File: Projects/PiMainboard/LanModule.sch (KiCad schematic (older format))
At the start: 0 parts

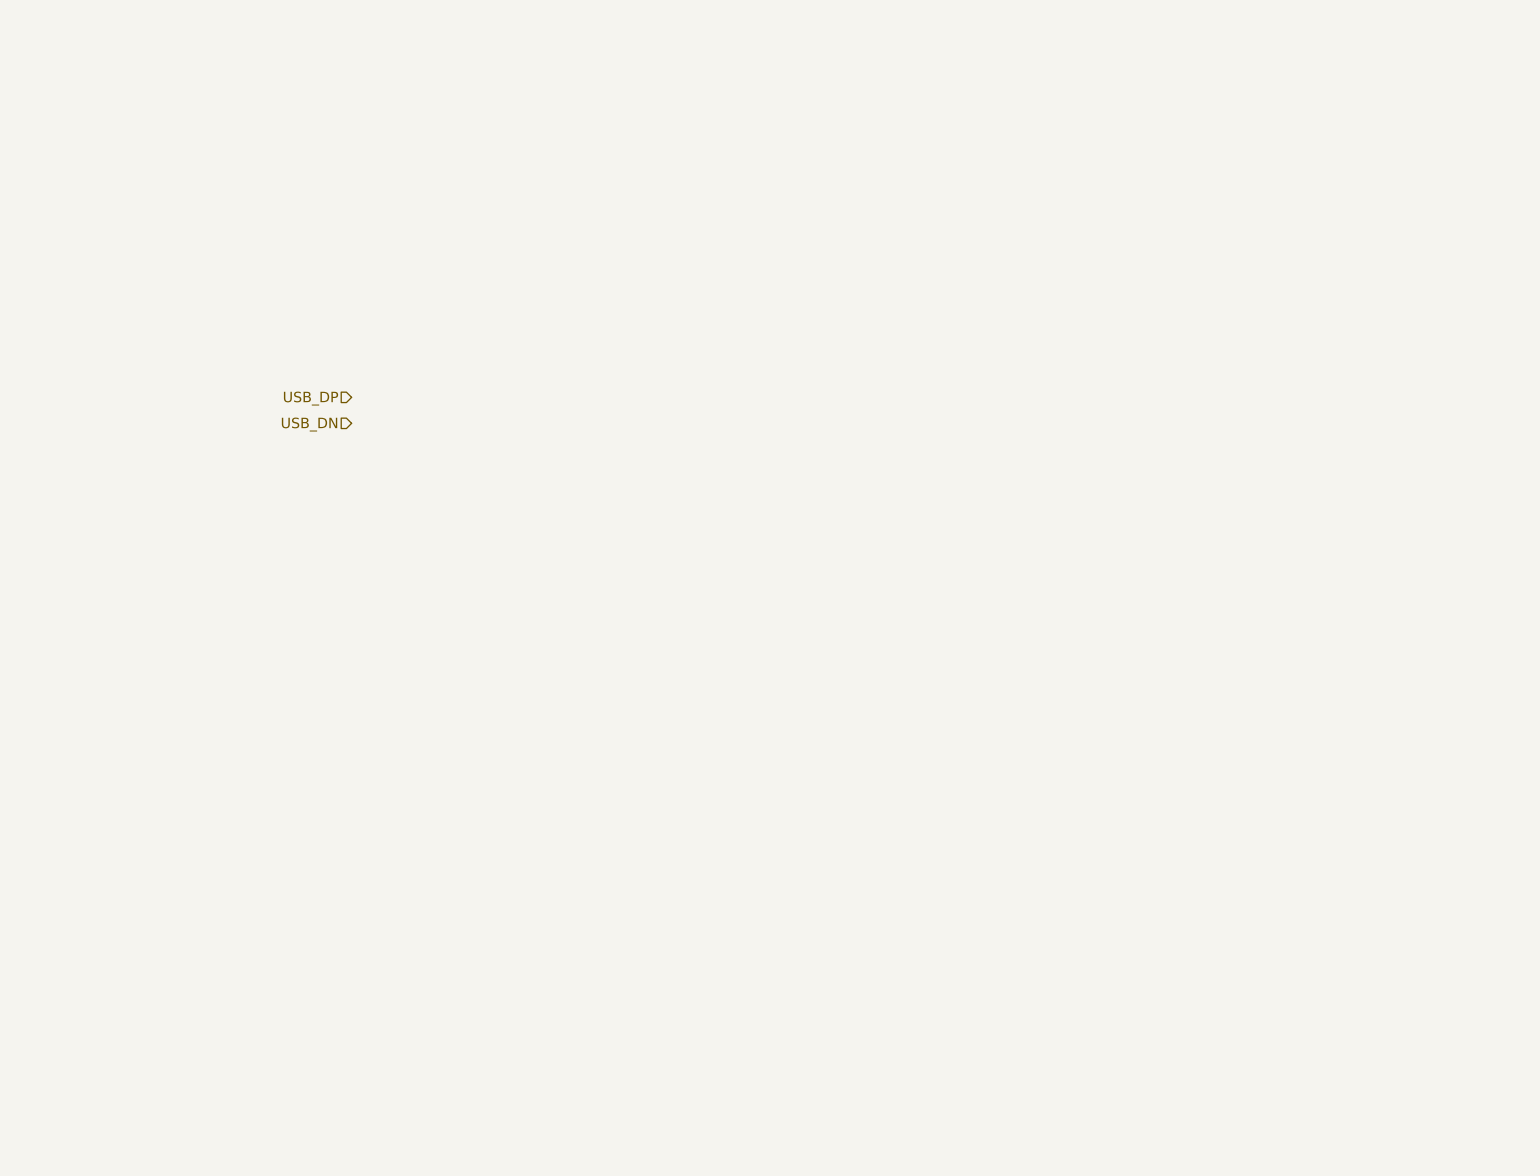
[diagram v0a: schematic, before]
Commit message: Added LAN to Pi board
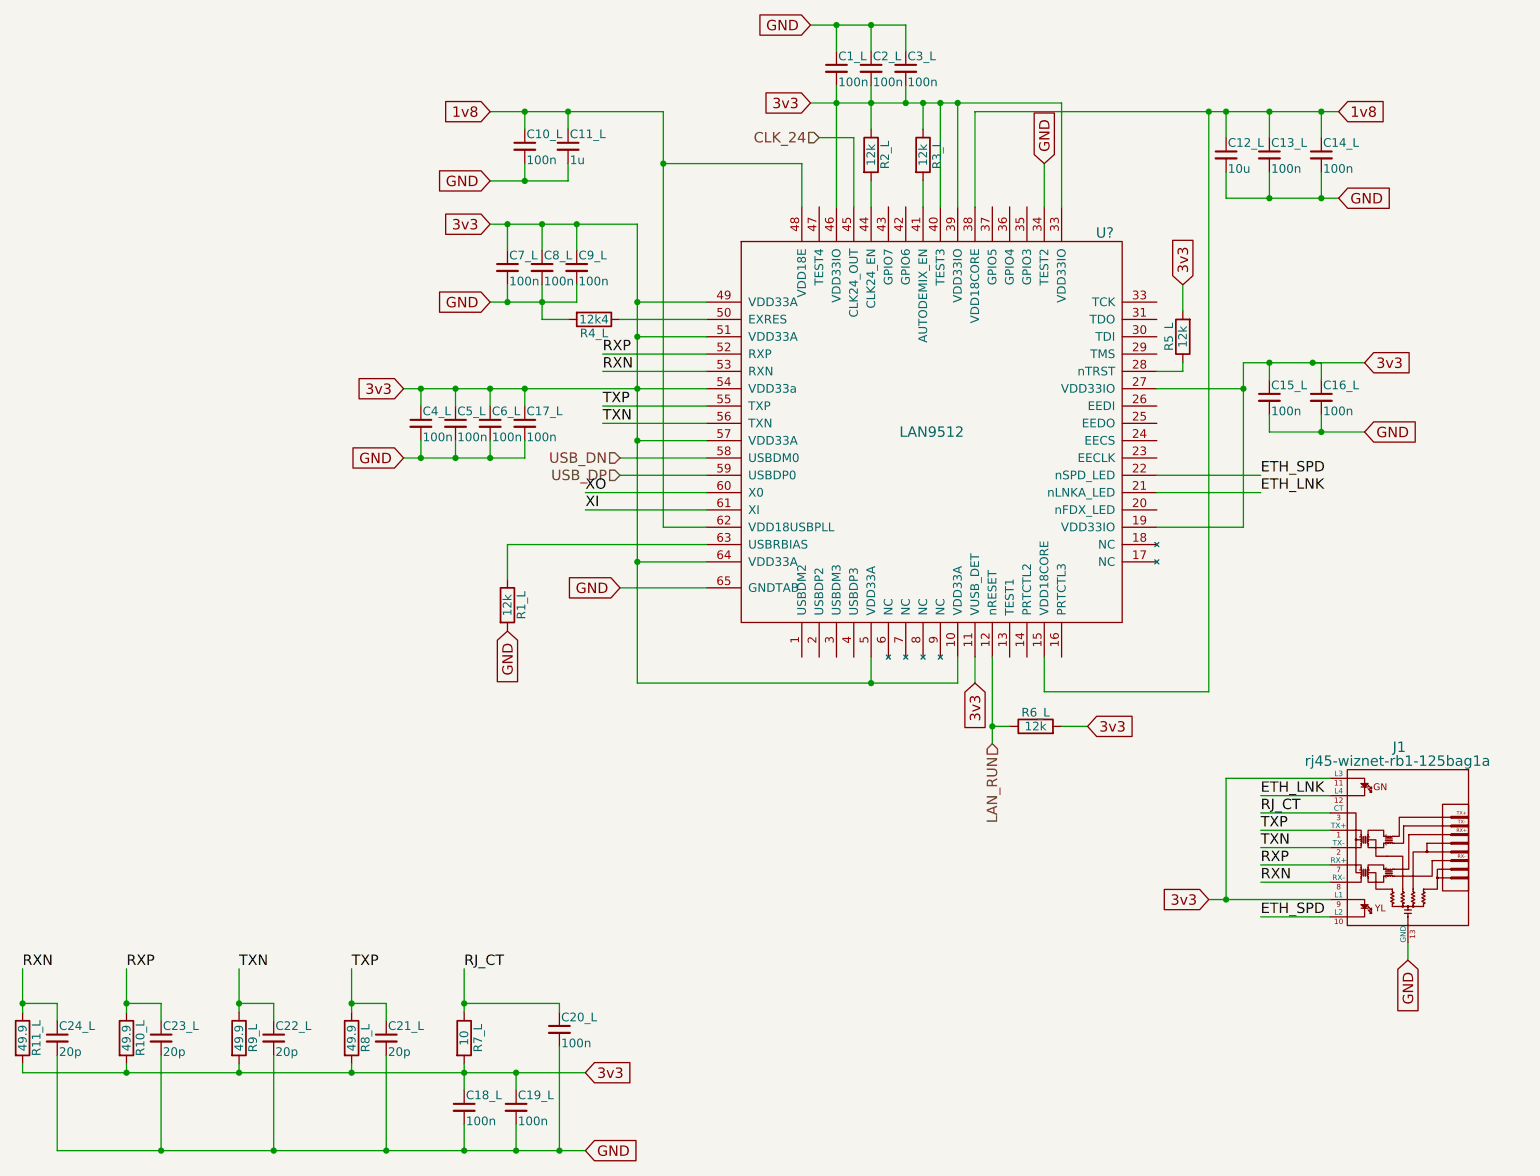
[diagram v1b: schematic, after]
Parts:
- added C10_L, C13_L, C14_L, C15_L, C16_L, C17_L, C18_L, C19_L, C1_L, C20_L, C2_L, C3_L, C4_L, C5_L, C6_L, C7_L, C8_L, C9_L: 100n, symbol C_Small
- added C11_L: 1u, symbol C_Small
- added C12_L: 10u, symbol C_Small
- added C21_L, C22_L, C23_L, C24_L: 20p, symbol C_Small
- added J1: rj45-wiznet-rb1-125bag1a, symbol rj45-wiznet-rb1-125bag1a
- added R10_L, R11_L, R8_L, R9_L: 49.9, symbol R
- added R1_L, R2_L, R3_L, R5_L, R6_L: 12k, symbol R
- added R4_L: 12k4, symbol R
- added R7_L: 10, symbol R
- added U?: LAN9512, symbol LAN9512
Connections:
- net USB_DN: now also U?.58 (USBDM0)
- net USB_DP: now also U?.59 (USBDP0)
- new net: R5_L.1, U?.28 (nTRST)
- new net: R3_L.2, U?.41 (AUTODEMIX_EN)
- new net: R2_L.2, U?.44 (CLK24_EN)
- new net: R4_L.1, U?.50 (EXRES)
- new net: R1_L.1, U?.63 (USBRBIAS)
- new net 1v8: C10_L.1, C11_L.1, C12_L.1, C13_L.1, C14_L.1, U?.15 (VDD18CORE), U?.38 (VDD18CORE), U?.48 (VDD18E), U?.62 (VDD18USBPLL)
- new net 3v3: C15_L.1, C16_L.1, C17_L.1, C18_L.1, C19_L.1, C1_L.2, C2_L.2, C3_L.2, C4_L.1, C5_L.1, C6_L.1, C7_L.1, C8_L.1, C9_L.1, J1.11 (L3), J1.9 (L1), R10_L.2, R11_L.2, R2_L.1, R3_L.1, R5_L.2, R6_L.2, R7_L.2, R8_L.2, R9_L.2, U?.10 (VDD33A), U?.11 (VUSB_DET), U?.19 (VDD33IO), U?.27 (VDD33IO), U?.33 (VDD33IO), U?.39 (VDD33IO), U?.40 (TEST3), U?.46 (VDD33IO), U?.49 (VDD33A), U?.5 (VDD33A), U?.51 (VDD33A), U?.54 (VDD33a), U?.57 (VDD33A), U?.64 (VDD33A)
- new net CLK_24: U?.45 (CLK24_OUT)
- new net ETH_LNK: J1.12 (L4), U?.21 (nLNKA_LED)
- new net ETH_SPD: J1.10 (L2), U?.22 (nSPD_LED)
- new net GND: C10_L.2, C11_L.2, C12_L.2, C13_L.2, C14_L.2, C15_L.2, C16_L.2, C17_L.2, C18_L.2, C19_L.2, C1_L.1, C20_L.2, C21_L.2, C22_L.2, C23_L.2, C24_L.2, C2_L.1, C3_L.1, C4_L.2, C5_L.2, C6_L.2, C7_L.2, C8_L.2, C9_L.2, J1.13 (GND), R1_L.2, R4_L.2, U?.34 (TEST2), U?.65 (GNDTAB)
- new net LAN_RUN: R6_L.1, U?.12 (nRESET)
- new net RJ_CT: C20_L.1, J1.3 (CT), R7_L.1
- new net RXN: C24_L.1, J1.8 (RX-), R11_L.1, U?.53 (RXN)
- new net RXP: C23_L.1, J1.7 (RX+), R10_L.1, U?.52 (RXP)
- new net TXN: C22_L.1, J1.2 (TX-), R9_L.1, U?.56 (TXN)
- new net TXP: C21_L.1, J1.1 (TX+), R8_L.1, U?.55 (TXP)
- new net XI: U?.61 (XI)
- new net XO: U?.60 (X0)

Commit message: Added PI CM IO "shield"
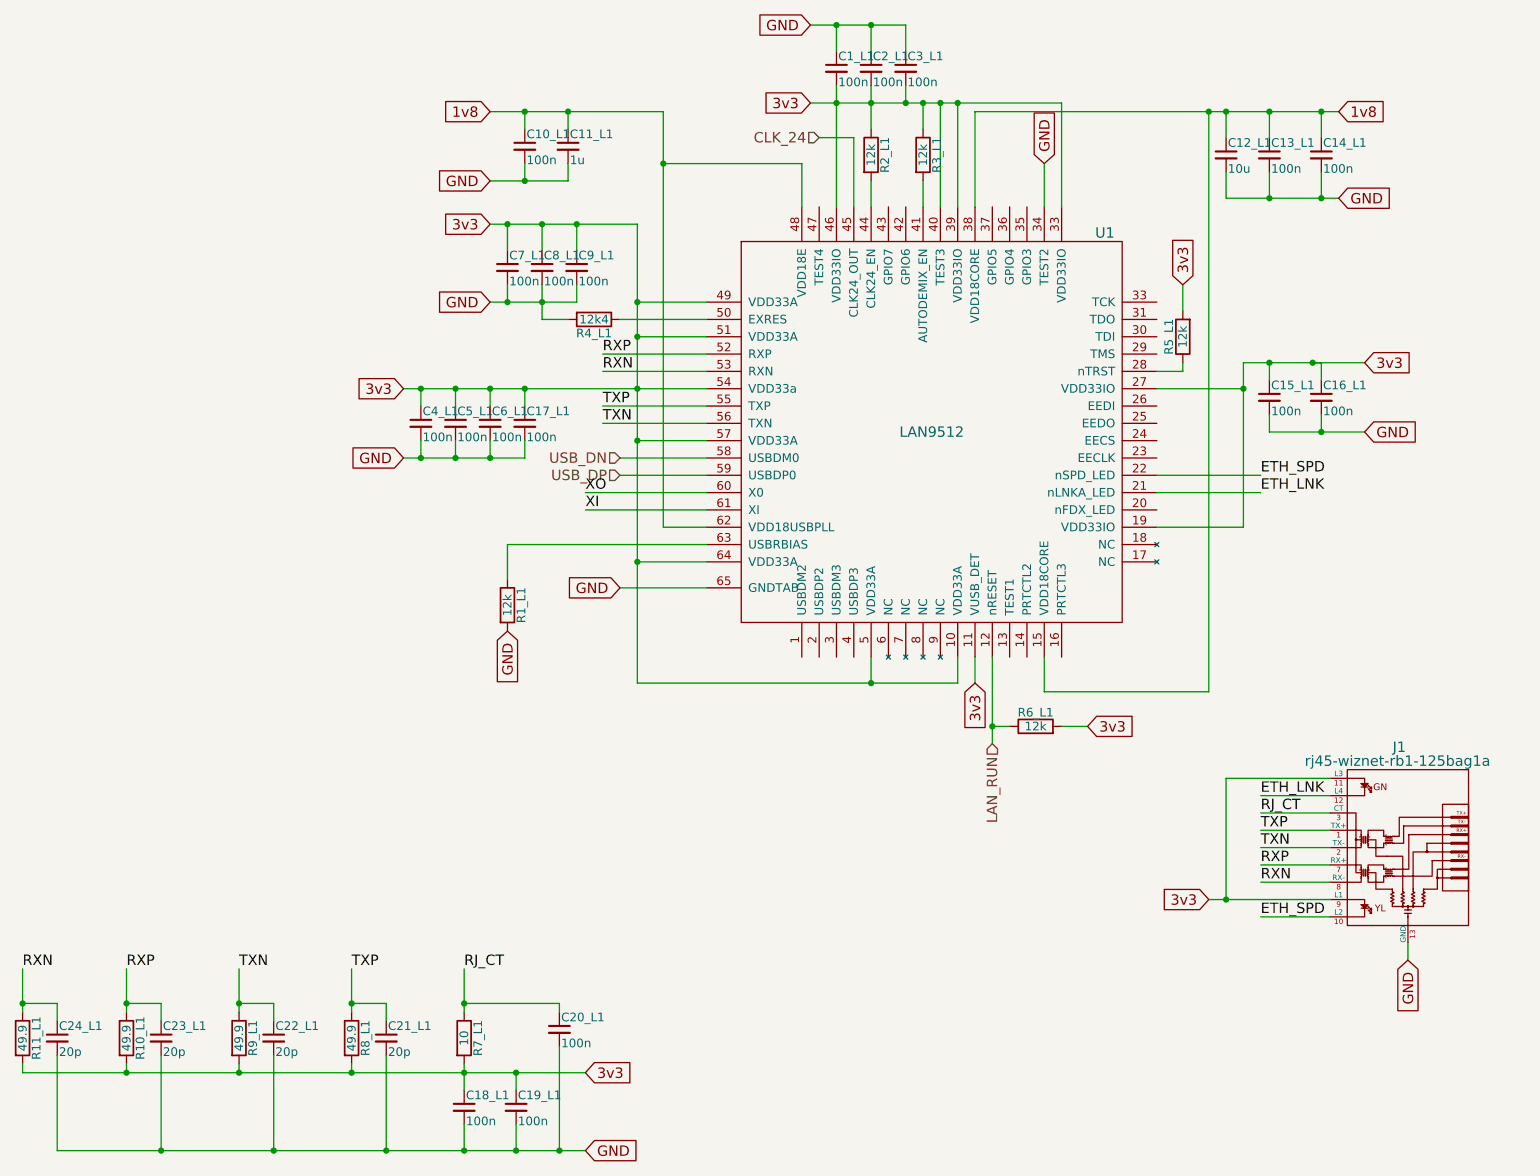
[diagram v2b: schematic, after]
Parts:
- gave numbers to parts that had none: 1
- renumbered C10_L to C10_L1, C11_L to C11_L1, C12_L to C12_L1, C13_L to C13_L1, C14_L to C14_L1, C15_L to C15_L1, C16_L to C16_L1, C17_L to C17_L1, C18_L to C18_L1, C19_L to C19_L1, C1_L to C1_L1, C20_L to C20_L1, C21_L to C21_L1, C22_L to C22_L1, C23_L to C23_L1, C24_L to C24_L1, C2_L to C2_L1, C3_L to C3_L1, C4_L to C4_L1, C5_L to C5_L1, C6_L to C6_L1, C7_L to C7_L1, C8_L to C8_L1, C9_L to C9_L1, R10_L to R10_L1, R11_L to R11_L1, R1_L to R1_L1, R2_L to R2_L1, R3_L to R3_L1, R4_L to R4_L1, R5_L to R5_L1, R6_L to R6_L1, R7_L to R7_L1, R8_L to R8_L1, R9_L to R9_L1
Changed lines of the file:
@@
 $Descr A4 11693 8268
 encoding utf-8
-Sheet 2 7
+Sheet 2 10
 Title ""
 Date ""
@@
 USB_DN
 $Comp
-L LAN9512 U?
+L LAN9512 U1
 U 1 1 567BBE0D
 P 7650 3000
-F 0 "U?" H 8650 4150 60  0000 C CNN
+F 0 "U1" H 8650 4150 60  0000 C CNN
 F 1 "LAN9512" H 7650 3000 60  0000 C CNN
 F 2 "" H 8100 2750 60  0000 C CNN
@@
 LAN_RUN
 $Comp
-L C_Small C1_L
+L C_Small C1_L1
 U 1 1 567BCBC3
 P 7100 900
-F 0 "C1_L" H 7110 970 50  0000 L CNN
+F 0 "C1_L1" H 7110 970 50  0000 L CNN
 F 1 "100n" H 7110 820 50  0000 L CNN
 F 2 "" H 7100 900 60  0000 C CNN
@@
 $EndComp
 $Comp
-L C_Small C2_L
+L C_Small C2_L1
 U 1 1 567BCC4E
 P 7300 900
-F 0 "C2_L" H 7310 970 50  0000 L CNN
+F 0 "C2_L1" H 7310 970 50  0000 L CNN
 F 1 "100n" H 7310 820 50  0000 L CNN
 F 2 "" H 7300 900 60  0000 C CNN
@@
 $EndComp
 $Comp
-L C_Small C3_L
+L C_Small C3_L1
 U 1 1 567BCC7D
 P 7500 900
-F 0 "C3_L" H 7510 970 50  0000 L CNN
+F 0 "C3_L1" H 7510 970 50  0000 L CNN
 F 1 "100n" H 7510 820 50  0000 L CNN
 F 2 "" H 7500 900 60  0000 C CNN
@@
 GND
 $Comp
-L C_Small C4_L
+L C_Small C4_L1
 U 1 1 567BD4D0
 P 4700 2950
-F 0 "C4_L" H 4710 3020 50  0000 L CNN
+F 0 "C4_L1" H 4710 3020 50  0000 L CNN
 F 1 "100n" H 4710 2870 50  0000 L CNN
 F 2 "" H 4700 2950 60  0000 C CNN
@@
 $EndComp
 $Comp
-L C_Small C5_L
+L C_Small C5_L1
 U 1 1 567BD563
 P 4900 2950
-F 0 "C5_L" H 4910 3020 50  0000 L CNN
+F 0 "C5_L1" H 4910 3020 50  0000 L CNN
 F 1 "100n" H 4910 2870 50  0000 L CNN
 F 2 "" H 4900 2950 60  0000 C CNN
@@
 $EndComp
 $Comp
-L C_Small C6_L
+L C_Small C6_L1
 U 1 1 567BD5AE
 P 5100 2950
-F 0 "C6_L" H 5110 3020 50  0000 L CNN
+F 0 "C6_L1" H 5110 3020 50  0000 L CNN
 F 1 "100n" H 5110 2870 50  0000 L CNN
 F 2 "" H 5100 2950 60  0000 C CNN
@@
 GND
 $Comp
-L R R1_L
+L R R1_L1
 U 1 1 567BDB10
 P 5200 4000
-F 0 "R1_L" V 5280 4000 50  0000 C CNN
+F 0 "R1_L1" V 5280 4000 50  0000 C CNN
 F 1 "12k" V 5200 4000 50  0000 C CNN
 F 2 "" V 5130 4000 30  0000 C CNN
@@
 3v3
 $Comp
-L R R3_L
+L R R3_L1
 U 1 1 567BE6EE
 P 7600 1400
-F 0 "R3_L" V 7680 1400 50  0000 C CNN
+F 0 "R3_L1" V 7680 1400 50  0000 C CNN
 F 1 "12k" V 7600 1400 50  0000 C CNN
 F 2 "" V 7530 1400 30  0000 C CNN
@@
 $EndComp
 $Comp
-L R R2_L
+L R R2_L1
 U 1 1 567BE7AA
 P 7300 1400
-F 0 "R2_L" V 7380 1400 50  0000 C CNN
+F 0 "R2_L1" V 7380 1400 50  0000 C CNN
 F 1 "12k" V 7300 1400 50  0000 C CNN
 F 2 "" V 7230 1400 30  0000 C CNN
@@
 $EndComp
 $Comp
-L C_Small C7_L
+L C_Small C7_L1
 U 1 1 567BF03B
 P 5200 2050
-F 0 "C7_L" H 5210 2120 50  0000 L CNN
+F 0 "C7_L1" H 5210 2120 50  0000 L CNN
 F 1 "100n" H 5210 1970 50  0000 L CNN
 F 2 "" H 5200 2050 60  0000 C CNN
@@
 $EndComp
 $Comp
-L C_Small C8_L
+L C_Small C8_L1
 U 1 1 567BF0BE
 P 5400 2050
-F 0 "C8_L" H 5410 2120 50  0000 L CNN
+F 0 "C8_L1" H 5410 2120 50  0000 L CNN
 F 1 "100n" H 5410 1970 50  0000 L CNN
 F 2 "" H 5400 2050 60  0000 C CNN
@@
 $EndComp
 $Comp
-L C_Small C9_L
+L C_Small C9_L1
 U 1 1 567BF0FE
 P 5600 2050
-F 0 "C9_L" H 5610 2120 50  0000 L CNN
+F 0 "C9_L1" H 5610 2120 50  0000 L CNN
 F 1 "100n" H 5610 1970 50  0000 L CNN
 F 2 "" H 5600 2050 60  0000 C CNN
@@
 GND
 $Comp
-L R R4_L
+L R R4_L1
 U 1 1 567BF80F
 P 5700 2350
-F 0 "R4_L" V 5780 2350 50  0000 C CNN
+F 0 "R4_L1" V 5780 2350 50  0000 C CNN
 F 1 "12k4" V 5700 2350 50  0000 C CNN
 F 2 "" V 5630 2350 30  0000 C CNN
@@
 1v8
 $Comp
-L C_Small C10_L
+L C_Small C10_L1
 U 1 1 567C02F4
 P 5300 1350
-F 0 "C10_L" H 5310 1420 50  0000 L CNN
+F 0 "C10_L1" H 5310 1420 50  0000 L CNN
 F 1 "100n" H 5310 1270 50  0000 L CNN
 F 2 "" H 5300 1350 60  0000 C CNN
@@
 $EndComp
 $Comp
-L C_Small C11_L
+L C_Small C11_L1
 U 1 1 567C035D
 P 5550 1350
-F 0 "C11_L" H 5560 1420 50  0000 L CNN
+F 0 "C11_L1" H 5560 1420 50  0000 L CNN
 F 1 "1u" H 5560 1270 50  0000 L CNN
 F 2 "" H 5550 1350 60  0000 C CNN
@@
 GND
 $Comp
-L C_Small C13_L
+L C_Small C13_L1
 U 1 1 567C1001
 P 9600 1400
-F 0 "C13_L" H 9610 1470 50  0000 L CNN
+F 0 "C13_L1" H 9610 1470 50  0000 L CNN
 F 1 "100n" H 9610 1320 50  0000 L CNN
 F 2 "" H 9600 1400 60  0000 C CNN
@@
 $EndComp
 $Comp
-L C_Small C12_L
+L C_Small C12_L1
 U 1 1 567C107E
 P 9350 1400
-F 0 "C12_L" H 9360 1470 50  0000 L CNN
+F 0 "C12_L1" H 9360 1470 50  0000 L CNN
 F 1 "10u" H 9360 1320 50  0000 L CNN
 F 2 "" H 9350 1400 60  0000 C CNN
@@
 GND
 $Comp
-L C_Small C14_L
+L C_Small C14_L1
 U 1 1 567C1366
 P 9900 1400
-F 0 "C14_L" H 9910 1470 50  0000 L CNN
+F 0 "C14_L1" H 9910 1470 50  0000 L CNN
 F 1 "100n" H 9910 1320 50  0000 L CNN
 F 2 "" H 9900 1400 60  0000 C CNN
@@
 CLK_24
 $Comp
-L R R5_L
+L R R5_L1
 U 1 1 567C368A
 P 9100 2450
-F 0 "R5_L" V 9180 2450 50  0000 C CNN
+F 0 "R5_L1" V 9180 2450 50  0000 C CNN
 F 1 "12k" V 9100 2450 50  0000 C CNN
 F 2 "" V 9030 2450 30  0000 C CNN
@@
 3v3
 $Comp
-L C_Small C15_L
+L C_Small C15_L1
 U 1 1 567C45EF
 P 9600 2800
-F 0 "C15_L" H 9610 2870 50  0000 L CNN
+F 0 "C15_L1" H 9610 2870 50  0000 L CNN
 F 1 "100n" H 9610 2720 50  0000 L CNN
 F 2 "" H 9600 2800 60  0000 C CNN
@@
 $EndComp
 $Comp
-L C_Small C16_L
+L C_Small C16_L1
 U 1 1 567C46C9
 P 9900 2800
-F 0 "C16_L" H 9910 2870 50  0000 L CNN
+F 0 "C16_L1" H 9910 2870 50  0000 L CNN
 F 1 "100n" H 9910 2720 50  0000 L CNN
 F 2 "" H 9900 2800 60  0000 C CNN
@@
 3v3
 $Comp
-L C_Small C17_L
+L C_Small C17_L1
 U 1 1 567C5B66
 P 5300 2950
-F 0 "C17_L" H 5310 3020 50  0000 L CNN
+F 0 "C17_L1" H 5310 3020 50  0000 L CNN
 F 1 "100n" H 5310 2870 50  0000 L CNN
 F 2 "" H 5300 2950 60  0000 C CNN
@@
 $EndComp
 $Comp
-L R R6_L
+L R R6_L1
 U 1 1 567C7D7B
 P 8250 4700
-F 0 "R6_L" V 8330 4700 50  0000 C CNN
+F 0 "R6_L1" V 8330 4700 50  0000 C CNN
 F 1 "12k" V 8250 4700 50  0000 C CNN
 F 2 "" V 8180 4700 30  0000 C CNN
@@
 RJ_CT
 $Comp
-L C_Small C18_L
+L C_Small C18_L1
 U 1 1 567D0B27
 P 4950 6900
-F 0 "C18_L" H 4960 6970 50  0000 L CNN
+F 0 "C18_L1" H 4960 6970 50  0000 L CNN
 F 1 "100n" H 4960 6820 50  0000 L CNN
 F 2 "" H 4950 6900 60  0000 C CNN
@@
 $EndComp
 $Comp
-L R R7_L
+L R R7_L1
 U 1 1 567D0BCA
 P 4950 6500
-F 0 "R7_L" V 5030 6500 50  0000 C CNN
+F 0 "R7_L1" V 5030 6500 50  0000 C CNN
 F 1 "10" V 4950 6500 50  0000 C CNN
 F 2 "" V 4880 6500 30  0000 C CNN
@@
 $EndComp
 $Comp
-L C_Small C19_L
+L C_Small C19_L1
 U 1 1 567D11B7
 P 5250 6900
-F 0 "C19_L" H 5260 6970 50  0000 L CNN
+F 0 "C19_L1" H 5260 6970 50  0000 L CNN
 F 1 "100n" H 5260 6820 50  0000 L CNN
 F 2 "" H 5250 6900 60  0000 C CNN
@@
 RJ_CT
 $Comp
-L R R8_L
+L R R8_L1
 U 1 1 567D4001
 P 4300 6500
-F 0 "R8_L" V 4380 6500 50  0000 C CNN
+F 0 "R8_L1" V 4380 6500 50  0000 C CNN
 F 1 "49.9" V 4300 6500 50  0000 C CNN
 F 2 "" V 4230 6500 30  0000 C CNN
@@
 $EndComp
 $Comp
-L R R9_L
+L R R9_L1
 U 1 1 567D42EE
 P 3650 6500
-F 0 "R9_L" V 3730 6500 50  0000 C CNN
+F 0 "R9_L1" V 3730 6500 50  0000 C CNN
 F 1 "49.9" V 3650 6500 50  0000 C CNN
 F 2 "" V 3580 6500 30  0000 C CNN
@@
 $EndComp
 $Comp
-L R R10_L
+L R R10_L1
 U 1 1 567D4367
 P 3000 6500
-F 0 "R10_L" V 3080 6500 50  0000 C CNN
+F 0 "R10_L1" V 3080 6500 50  0000 C CNN
 F 1 "49.9" V 3000 6500 50  0000 C CNN
 F 2 "" V 2930 6500 30  0000 C CNN
@@
 $EndComp
 $Comp
-L R R11_L
+L R R11_L1
 U 1 1 567D441C
 P 2400 6500
-F 0 "R11_L" V 2480 6500 50  0000 C CNN
+F 0 "R11_L1" V 2480 6500 50  0000 C CNN
 F 1 "49.9" V 2400 6500 50  0000 C CNN
 F 2 "" V 2330 6500 30  0000 C CNN
@@
 $EndComp
 $Comp
-L C_Small C20_L
+L C_Small C20_L1
 U 1 1 567D4862
 P 5500 6450
-F 0 "C20_L" H 5510 6520 50  0000 L CNN
+F 0 "C20_L1" H 5510 6520 50  0000 L CNN
 F 1 "100n" H 5510 6370 50  0000 L CNN
 F 2 "" H 5500 6450 60  0000 C CNN
@@
 $EndComp
 $Comp
-L C_Small C21_L
+L C_Small C21_L1
 U 1 1 567D6EAB
 P 4500 6500
-F 0 "C21_L" H 4510 6570 50  0000 L CNN
+F 0 "C21_L1" H 4510 6570 50  0000 L CNN
 F 1 "20p" H 4510 6420 50  0000 L CNN
 F 2 "" H 4500 6500 60  0000 C CNN
@@
 $EndComp
 $Comp
-L C_Small C22_L
+L C_Small C22_L1
 U 1 1 567D707E
 P 3850 6500
-F 0 "C22_L" H 3860 6570 50  0000 L CNN
+F 0 "C22_L1" H 3860 6570 50  0000 L CNN
 F 1 "20p" H 3860 6420 50  0000 L CNN
 F 2 "" H 3850 6500 60  0000 C CNN
@@
 $EndComp
 $Comp
-L C_Small C23_L
+L C_Small C23_L1
 U 1 1 567D7226
 P 3200 6500
-F 0 "C23_L" H 3210 6570 50  0000 L CNN
+F 0 "C23_L1" H 3210 6570 50  0000 L CNN
 F 1 "20p" H 3210 6420 50  0000 L CNN
 F 2 "" H 3200 6500 60  0000 C CNN
@@
 $EndComp
 $Comp
-L C_Small C24_L
+L C_Small C24_L1
 U 1 1 567D738D
 P 2600 6500
-F 0 "C24_L" H 2610 6570 50  0000 L CNN
+F 0 "C24_L1" H 2610 6570 50  0000 L CNN
 F 1 "20p" H 2610 6420 50  0000 L CNN
 F 2 "" H 2600 6500 60  0000 C CNN
